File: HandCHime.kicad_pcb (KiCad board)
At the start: 4 copper layers, 38.1 x 22.6 mm, 18 parts, among them J1 USB_C_Receptacle_USB2.0, J2 Pins, SW0 BOOT, SW1 Row 0, Col 0, SW2 Row 0, Col 1, U1 CH552T, U2 PRTR5V0U2X

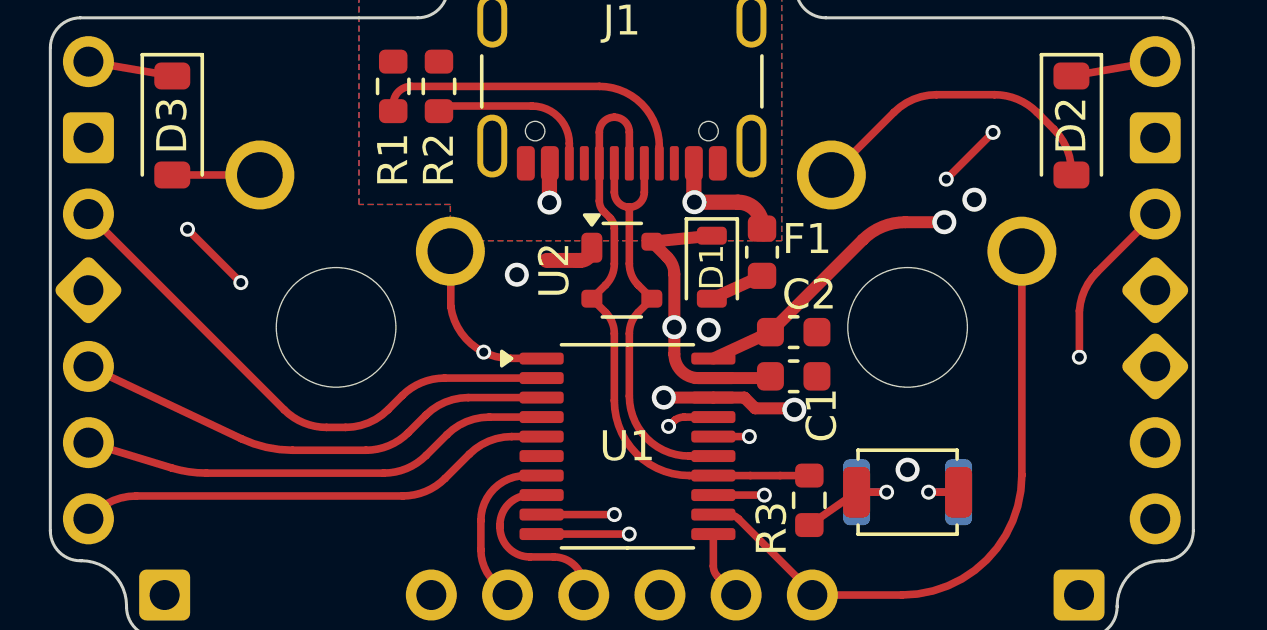
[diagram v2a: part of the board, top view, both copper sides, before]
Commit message: Move vias away from pin labels
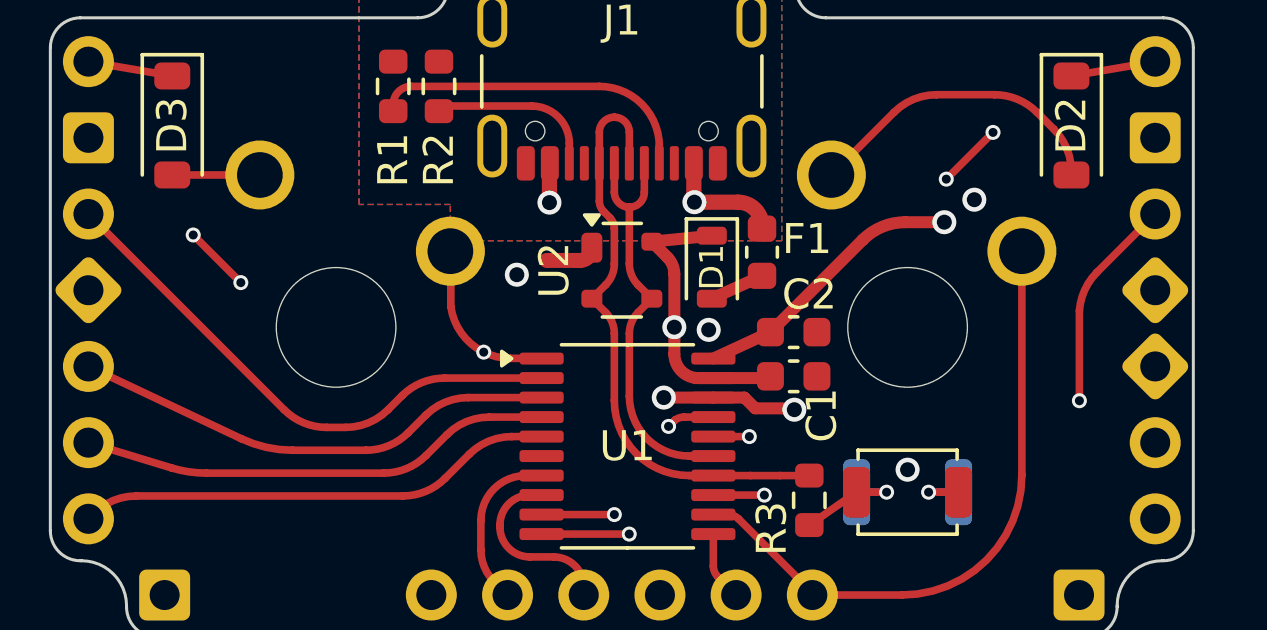
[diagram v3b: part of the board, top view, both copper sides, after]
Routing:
- net P35: track 20.2 -> 21.1 mm
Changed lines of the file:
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@@
+	)
+	(segment
+		(start 163.5 47)
+		(end 166.25 47)
+		(width 0.4)
+		(layer "In2.Cu")
+		(net 1)
+	)
+	(segment
+		(start 172.147 44.385)
+		(end 176.53 48.768)
+		(width 0.4)
+		(layer "In2.Cu")
+		(net 1)
+	)
+	(segment
+		(start 149.866858 46.841355)
+		(end 146.198645 46.841355)
+		(width 0.4)
+		(layer "In2.Cu")
+		(net 1)
+	)
+	(segment
+		(start 146.198645 46.841355)
+		(end 144.272 48.768)
+		(width 0.4)
+		(layer "In2.Cu")
+		(net 1)
+	)
+	(segment
+		(start 160.5 50)
+		(end 157 50)
+		(width 0.4)
+		(layer "In2.Cu")
+		(net 1)
 	)
 	(segment
@@
 	)
 	(segment
-		(start 143.764 48.768)
-		(end 140.97 48.768)
-		(width 0.4)
-		(layer "In2.Cu")
-		(net 1)
-	)
-	(segment
-		(start 160.5 50)
-		(end 157 50)
-		(width 0.4)
-		(layer "In2.Cu")
-		(net 1)
-	)
-	(segment
-		(start 163.5 47)
-		(end 166.25 47)
-		(width 0.4)
-		(layer "In2.Cu")
-		(net 1)
-	)
-	(segment
 		(start 156.25 49.25)
 		(end 152.275503 49.25)
@@
 	)
 	(segment
+		(start 160.5 50)
+		(end 163.5 47)
+		(width 0.4)
+		(layer "In2.Cu")
+		(net 1)
+	)
+	(segment
 		(start 157 50)
 		(end 156.25 49.25)
@@
 	)
 	(segment
-		(start 172.147 44.385)
-		(end 176.53 48.768)
-		(width 0.4)
-		(layer "In2.Cu")
-		(net 1)
-	)
-	(segment
-		(start 160.5 50)
-		(end 163.5 47)
-		(width 0.4)
-		(layer "In2.Cu")
-		(net 1)
-	)
-	(segment
-		(start 149.866858 46.841355)
-		(end 145.690645 46.841355)
-		(width 0.4)
-		(layer "In2.Cu")
-		(net 1)
-	)
-	(segment
 		(start 166.25 47)
 		(end 168.865 44.385)
@@
 	)
 	(segment
-		(start 145.690645 46.841355)
-		(end 143.764 48.768)
+		(start 144.272 48.768)
+		(end 140.97 48.768)
 		(width 0.4)
 		(layer "In2.Cu")
@@
 	)
 	(segment
+		(start 169.9412 54.5338)
+		(end 173.3042 54.5338)
+		(width 0.254)
+		(layer "In2.Cu")
+		(net 7)
+	)
+	(segment
 		(start 175.222 50)
 		(end 176.53 51.308)
@@
 	)
 	(segment
-		(start 168.975 55.5)
-		(end 169.475 55)
-		(width 0.254)
-		(layer "In2.Cu")
-		(net 7)
-	)
-	(segment
 		(start 169.5 46.5)
 		(end 169.5 47.5)
@@
 	)
 	(segment
+		(start 168.975 55.5)
+		(end 169.9412 54.5338)
+		(width 0.254)
+		(layer "In2.Cu")
+		(net 7)
+	)
+	(segment
 		(start 169.5 47.5)
 		(end 172 50)
@@
 	)
 	(segment
-		(start 169.475 55)
-		(end 172.838 55)
-		(width 0.254)
-		(layer "In2.Cu")
-		(net 7)
-	)
-	(segment
 		(start 172 50)
 		(end 175.222 50)
@@
 	)
 	(segment
-		(start 172.838 55)
+		(start 173.3042 54.5338)
 		(end 176.53 51.308)
 		(width 0.254)
@@
 	)
 	(segment
+		(start 146.05 48.514)
+		(end 144.4625 46.9265)
+		(width 0.254)
+		(layer "F.Cu")
+		(net 9)
+	)
+	(segment
 		(start 160.307 53.307)
 		(end 160.308918 53.307)
@@
 		(start 160.308918 53.307)
 		(end 160.518933 53.096985)
-		(width 0.254)
-		(layer "F.Cu")
-		(net 9)
-	)
-	(segment
-		(start 146.05 48.514)
-		(end 144.272 46.736)
 		(width 0.254)
 		(layer "F.Cu")
@@
 	)
 	(via
-		(at 144.272 46.736)
+		(at 144.4625 46.9265)
 		(size 0.5)
 		(drill 0.3)
@@
 	)
 	(segment
-		(start 144.272 44.45)
-		(end 140.97 41.148)
-		(width 0.254)
-		(layer "In2.Cu")
-		(net 9)
-	)
-	(segment
 		(start 155.58457 50.17457)
 		(end 158.717 53.307)
@@
 	)
 	(segment
-		(start 144.272 46.736)
-		(end 144.272 44.45)
+		(start 144.4625 46.9265)
+		(end 144.4625 44.6405)
 		(width 0.254)
 		(layer "In2.Cu")
@@
 		(start 171.122556 43.507444)
 		(end 173.482 41.148)
+		(width 0.254)
+		(layer "In2.Cu")
+		(net 9)
+	)
+	(segment
+		(start 144.4625 44.6405)
+		(end 140.97 41.148)
 		(width 0.254)
 		(layer "In2.Cu")
@@
 	)
 	(segment
+		(start 174 52.451)
+		(end 174.001906 52.449094)
+		(width 0.254)
+		(layer "F.Cu")
+		(net 30)
+	)
+	(segment
+		(start 163.5 55.59717)
+		(end 163.49883 55.596)
+		(width 0.254)
+		(layer "F.Cu")
+		(net 30)
+	)
+	(segment
 		(start 174.585787 48.172213)
 		(end 176.53 46.228)
@@
 	)
 	(segment
-		(start 174.001906 50.998094)
+		(start 174.001906 52.449094)
 		(end 174.001906 49.455464)
-		(width 0.254)
-		(layer "F.Cu")
-		(net 30)
-	)
-	(segment
-		(start 163.5 55.59717)
-		(end 163.49883 55.596)
-		(width 0.254)
-		(layer "F.Cu")
-		(net 30)
-	)
-	(segment
-		(start 174 51)
-		(end 174.001906 50.998094)
 		(width 0.254)
 		(layer "F.Cu")
@@
 	)
 	(via
-		(at 174 51)
+		(at 174.001906 52.451)
 		(size 0.5)
 		(drill 0.3)
@@
 	)
 	(segment
-		(start 165.05417 54.043)
+		(start 174 52.452906)
+		(end 173.189106 53.2638)
+		(width 0.254)
+		(layer "In2.Cu")
+		(net 30)
+	)
+	(segment
+		(start 174 52.451)
+		(end 174 52.452906)
+		(width 0.254)
+		(layer "In2.Cu")
+		(net 30)
+	)
+	(segment
+		(start 173.189106 53.2638)
+		(end 165.83337 53.2638)
+		(width 0.254)
+		(layer "In2.Cu")
+		(net 30)
+	)
+	(segment
+		(start 165.83337 53.2638)
 		(end 163.5 55.59717)
 		(width 0.254)
 		(layer "In2.Cu")
-		(net 30)
-	)
-	(segment
-		(start 174 51)
-		(end 170.957 54.043)
-		(width 0.254)
-		(layer "In2.Cu")
-		(net 30)
-	)
-	(segment
-		(start 170.957 54.043)
-		(end 165.05417 54.043)
-		(width 0.254)
-		(layer "In2.Cu")

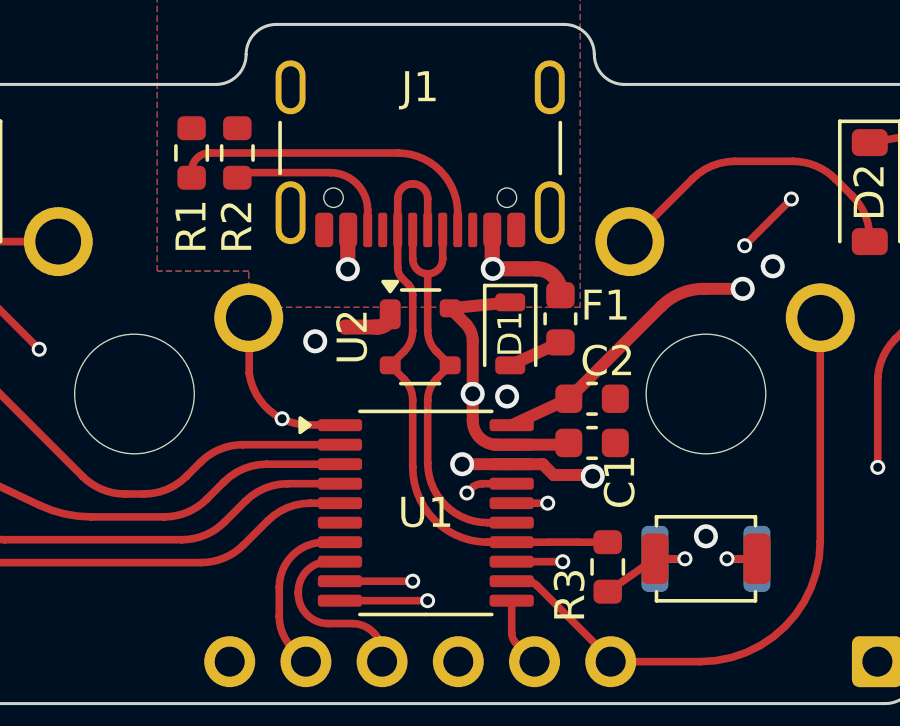
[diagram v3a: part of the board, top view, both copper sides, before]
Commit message: Redo USB D± routing
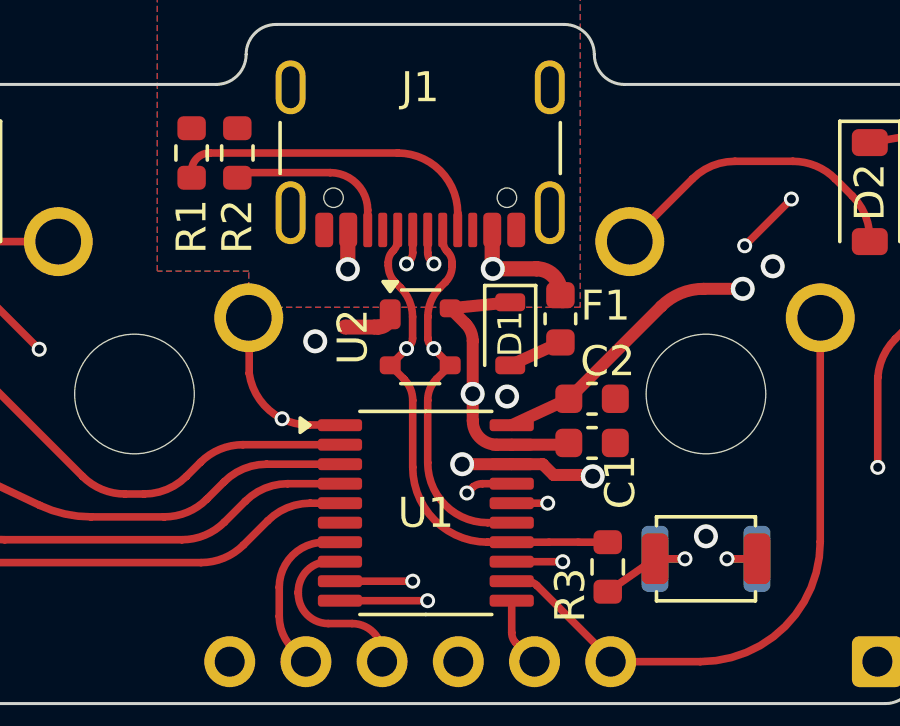
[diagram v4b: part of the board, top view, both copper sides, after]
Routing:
- net USB-: track 14.2 -> 16.8 mm, vias 0 -> 2
- net USB+: track 18.1 -> 19.0 mm, vias 0 -> 2
